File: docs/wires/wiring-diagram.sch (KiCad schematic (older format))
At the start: 15 parts, among them J101_powerboard DB15_MALE, J102_mainboard DB9_FEMALE, J103_mainboard DB9_FEMALE, J103_powerboard DB9_FEMALE, J104_powerboard DB15_FEMALE, J1_optical-distance_1 CONN_02X03, J1_optical-distance_3 CONN_02X03, J1_optical-distance_? CONN_02X03, J1_pressure-sensor CONN_01X04_MALE, J1_temperature-sensor-DS1731 CONN_01X04_MALE, J201_mainboard DB25_FEMALE, J801_powerboard DB25_FEMALE, U1201_mainboard DB_26, U201_mainboard DB_44, U202_mainboard DB_78

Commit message: wires: worked further at the wiring diagram
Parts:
- added J1_endswitch, J1_heatprobe_1, P1_camera-light_1, P1_camera-light_? (x2), P2_camera-light_1, P2_camera-light_? (x2): CONN_01X02, symbol CONN_01X02
- added J1_ltc3757_GND_1, J2_ltc3757_ENABLE_1, J3_ltc3757_BAT_1, J4_ltc3757_24V_1, J9_ltc3757_GND_1: CONN_01X01, symbol CONN_01X01
- added J1_motor: CONN_01X08, symbol CONN_01X08
- added J1_motor-encoder: CONN_01X10, symbol CONN_01X10
- added J1_temperature-sensor-DS1, J1_temperature-sensor-DS2, J1_temperature-sensor-DS3, J1_temperature-sensor-DS4: CONN_01X04_MALE, symbol CONN_01X04_MALE
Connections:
- net labels added: GND, Motor+, Motor-, bat_24V_1, bat_24V_2, bat_24V_3, motor-encoder_GND, motor-hall_5V, motor-hall_GND, motor-hall_U, motor-hall_V, motor-hall_W, probe_1, probe_2, probe_3, t1_RTD1_A, t1_RTD6_D, t2_RTD1_A, t2_RTD6_D, t3_RTD1_A, t3_RTD6_D, t4_RTD1_A, t4_RTD2_B, t4_RTD6_D, t5_RTD1_A, t5_RTD6_D, t6_RTD1_A, t6_RTD6_D
- net labels removed: +3V3, hall_U, hall_V, hall_W
- wire segments 121 -> 207
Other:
- note added: "+"
- note added: "-"
- note added: "BOARD: camera-light"
- note added: "BOARD: lt3757-boost-converter"
- note added: "End-Switch"
- note added: "FREEK Kleinheizpatrone 24V"
- note added: "Motor EC-max 22, 283840"
- note added: "Motor-Encoder MR Typ-M, 201937"
- moved on the sheet: J1_temperature-sensor-DS1731, U201_mainboard, U202_mainboard

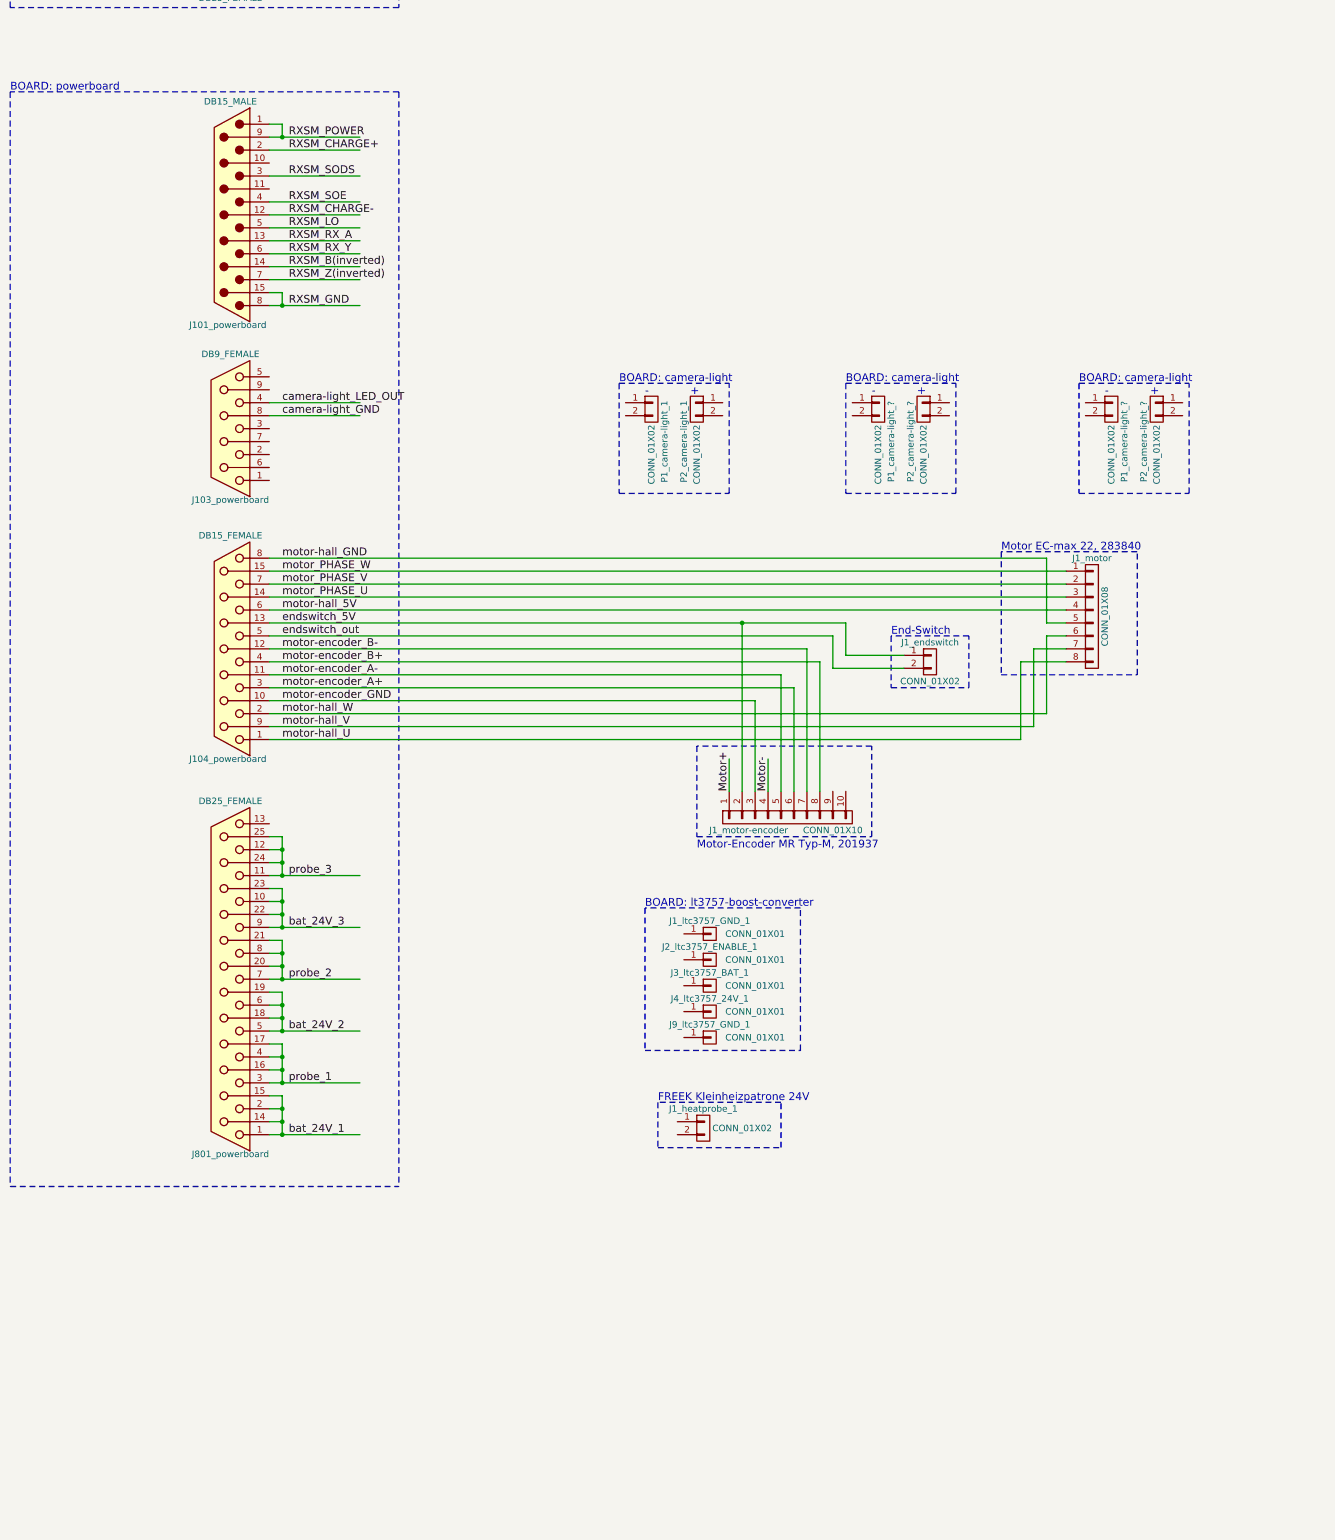
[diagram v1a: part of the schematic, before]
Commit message: wires: missing LEDS, Pi-Board
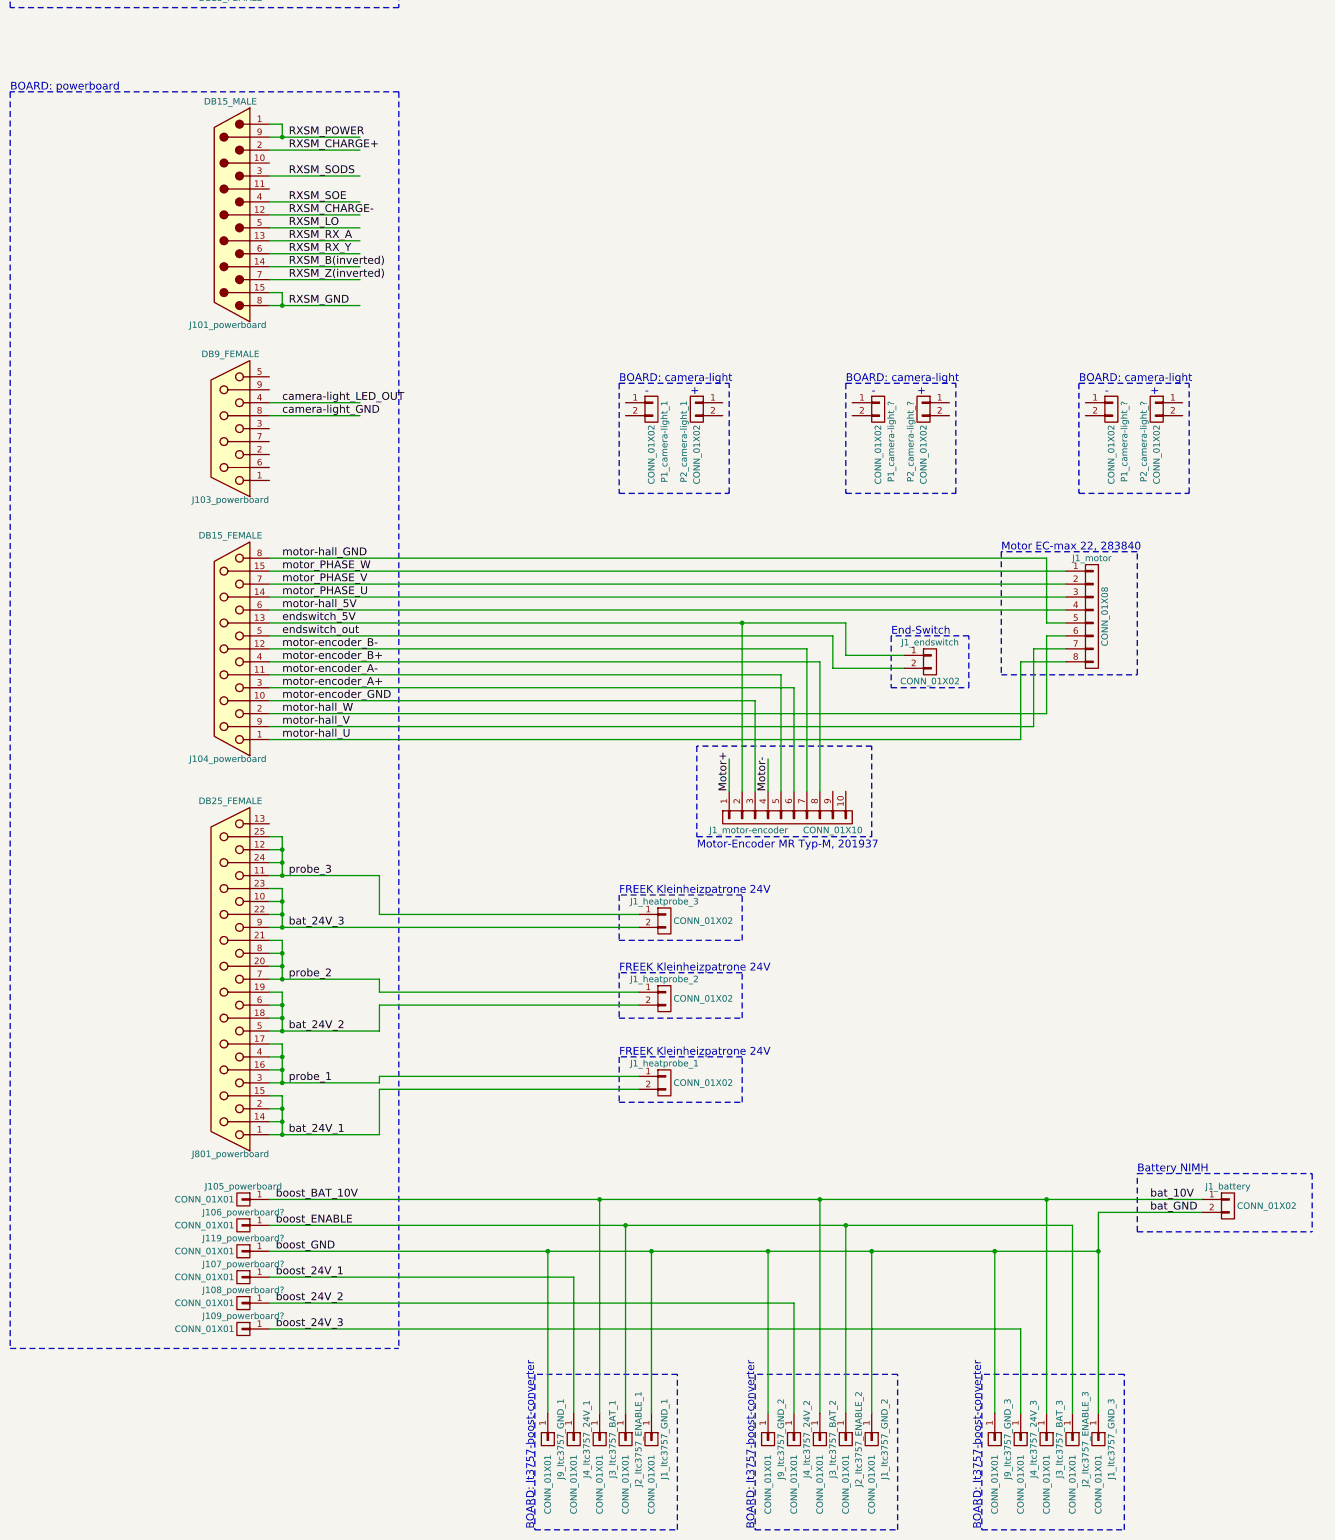
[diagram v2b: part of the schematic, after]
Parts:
- added J105_powerboard, J106_powerboard?, J107_powerboard?, J108_powerboard?, J109_powerboard?, J119_powerboard?, J1_ltc3757_GND_2, J1_ltc3757_GND_3, J2_ltc3757_ENABLE_2, J2_ltc3757_ENABLE_3, J3_ltc3757_BAT_2, J3_ltc3757_BAT_3, J4_ltc3757_24V_2, J4_ltc3757_24V_3, J9_ltc3757_GND_2, J9_ltc3757_GND_3: CONN_01X01, symbol CONN_01X01
- added J1_battery, J1_heatprobe_1, J1_heatprobe_2: CONN_01X02, symbol CONN_01X02
- renumbered J1_heatprobe_1 to J1_heatprobe_3
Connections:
- net labels added: bat_10V, bat_GND, boost_24V_1, boost_24V_2, boost_24V_3, boost_BAT_10V, boost_ENABLE, boost_GND
- wire segments 207 -> 239
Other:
- note added: "Battery NIMH"
- moved on the sheet: J1_heatprobe_3, J1_ltc3757_GND_1, J2_ltc3757_ENABLE_1, J3_ltc3757_BAT_1, J4_ltc3757_24V_1, J9_ltc3757_GND_1

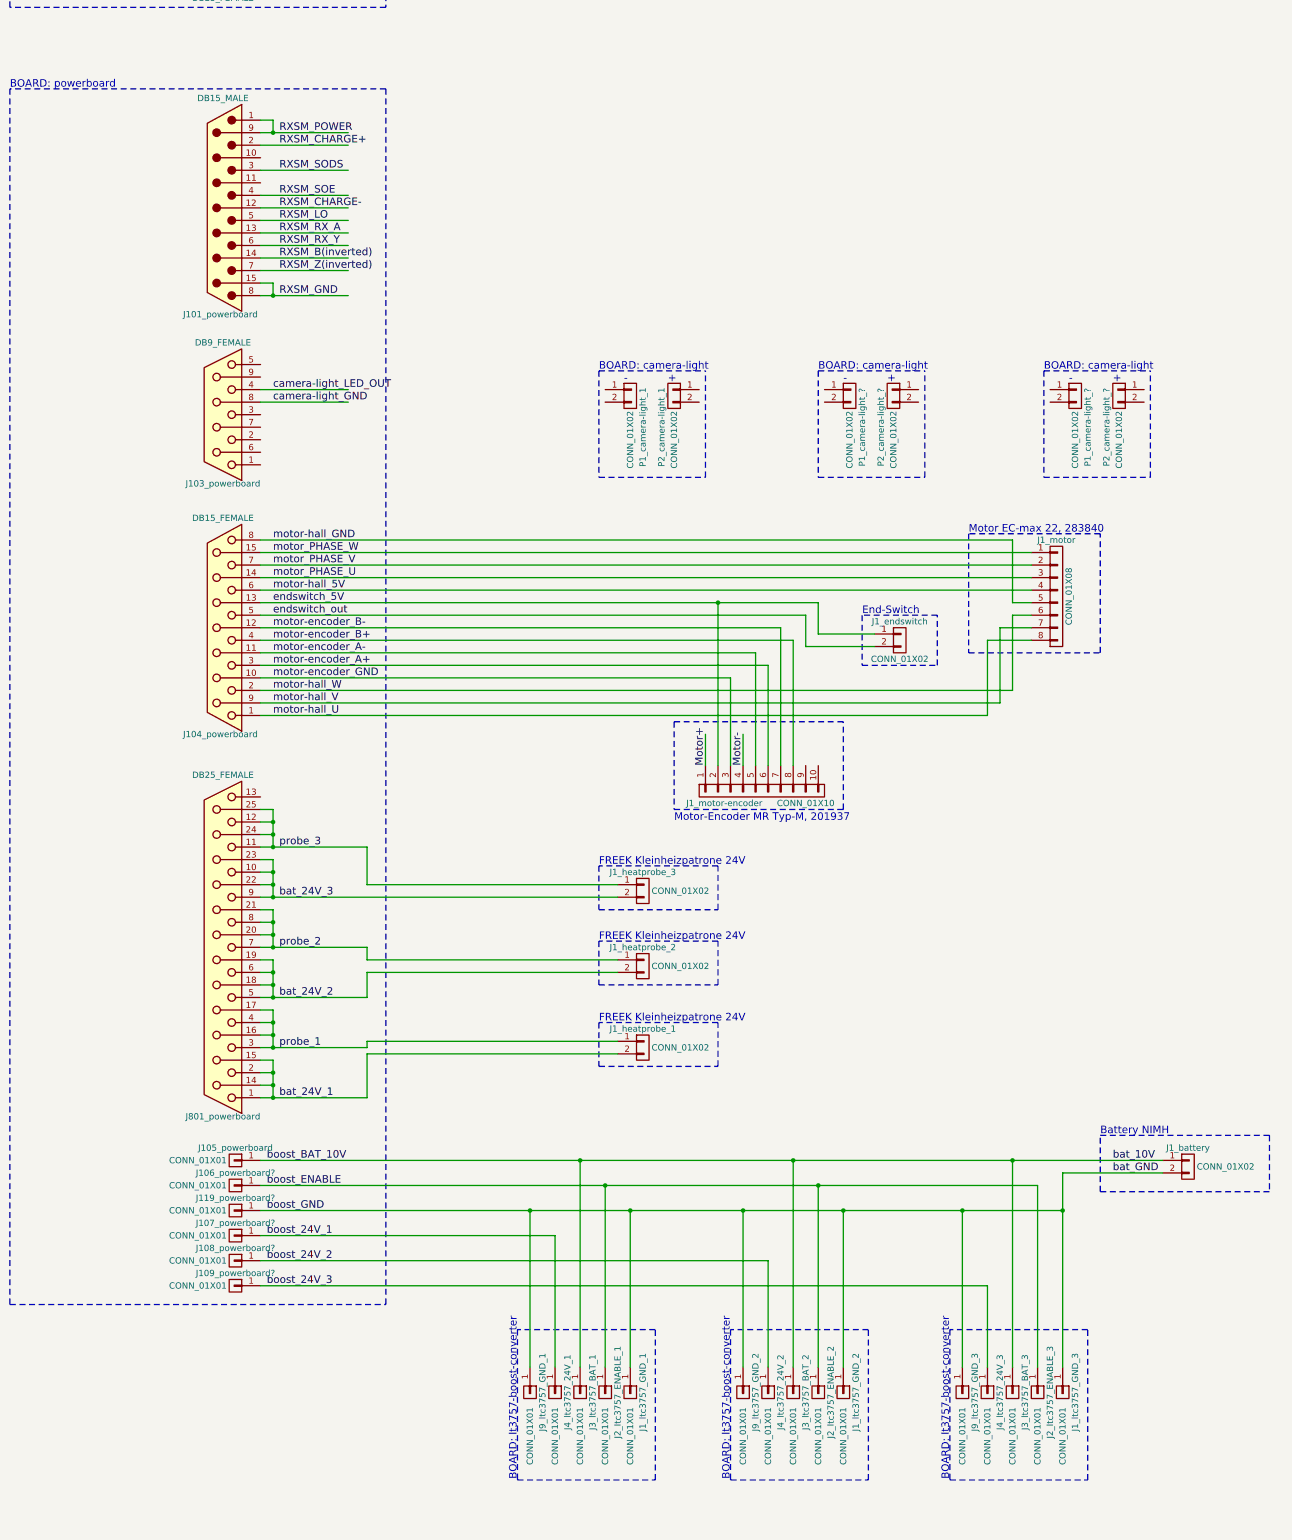
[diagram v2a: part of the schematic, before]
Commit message: wires: fixed boost converter wiring
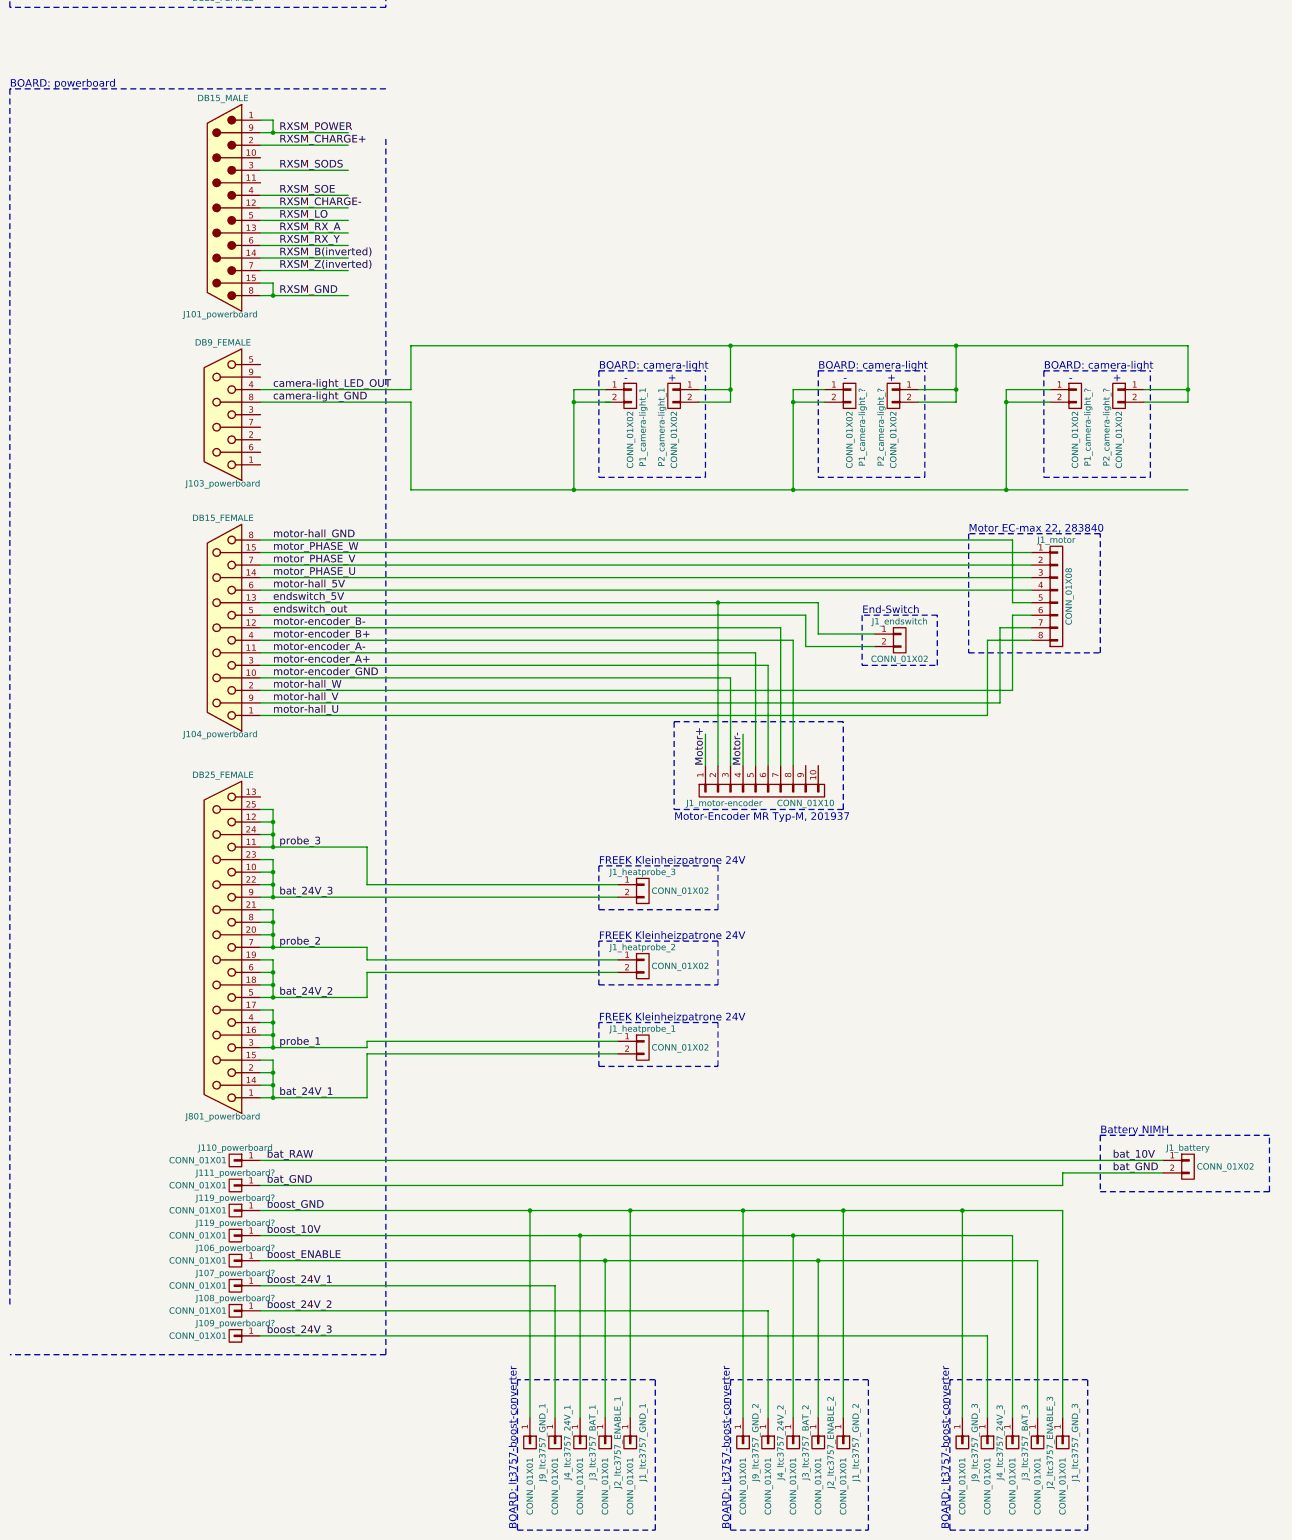
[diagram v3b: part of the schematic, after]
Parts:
- added J111_powerboard?, J119_powerboard?: CONN_01X01, symbol CONN_01X01
- renumbered J105_powerboard to J110_powerboard
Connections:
- net labels added: bat_RAW, boost_10V
- net labels removed: boost_BAT_10V
- wire segments 239 -> 264
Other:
- moved on the sheet: J106_powerboard?, J107_powerboard?, J108_powerboard?, J109_powerboard?, J1_ltc3757_GND_1, J1_ltc3757_GND_2, J1_ltc3757_GND_3, J2_ltc3757_ENABLE_1, J2_ltc3757_ENABLE_2, J2_ltc3757_ENABLE_3, J3_ltc3757_BAT_1, J3_ltc3757_BAT_2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
